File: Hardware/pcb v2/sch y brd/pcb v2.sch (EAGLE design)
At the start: 58 parts, among them J1 AVR_SPI_PRG_6PTH, J2 1981584-1, J3 HDMI, J4 JST-3, J5 HDMI, Q1 PMBT3904, Q2 PMBT3904, Q3 MC-306, U1 ATMEGA328P, U2 TXS0108EPWR-TSSOP20, U3 ADP3338AKCZ-3.3RL7, U4 DS1307SO8, Y1 CSTCE16M0V53-R0 16MHZ

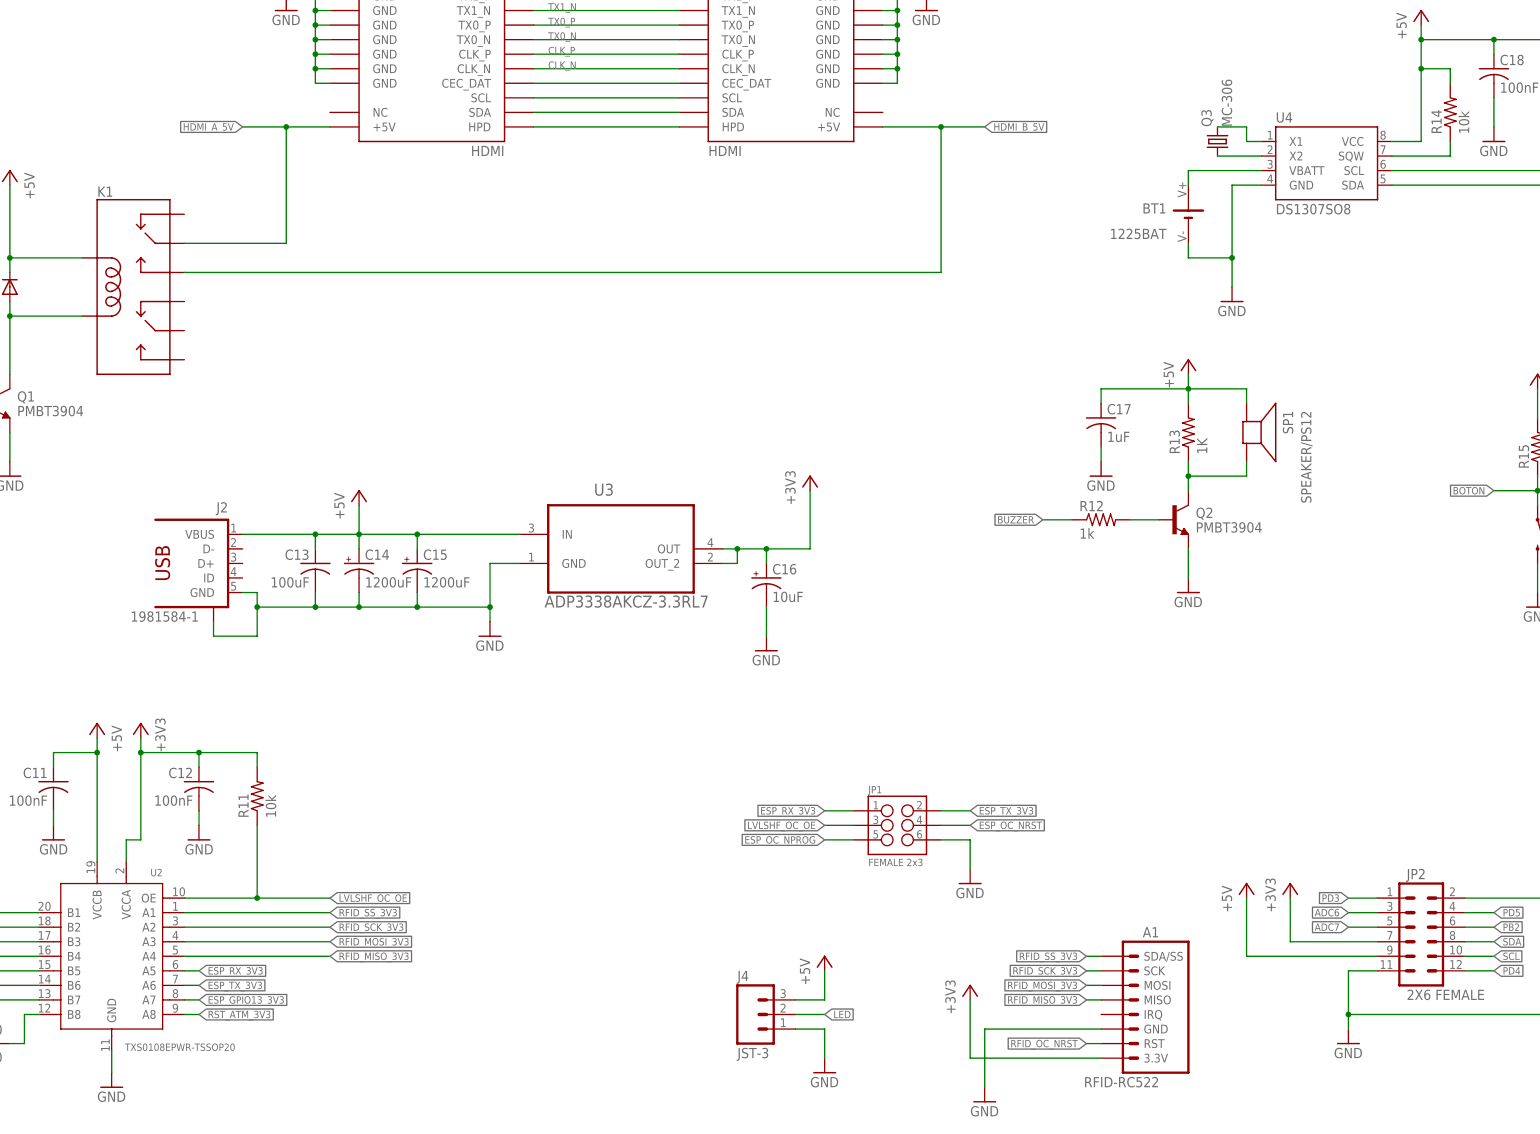
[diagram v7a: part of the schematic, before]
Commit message: Serigrafia arreglada
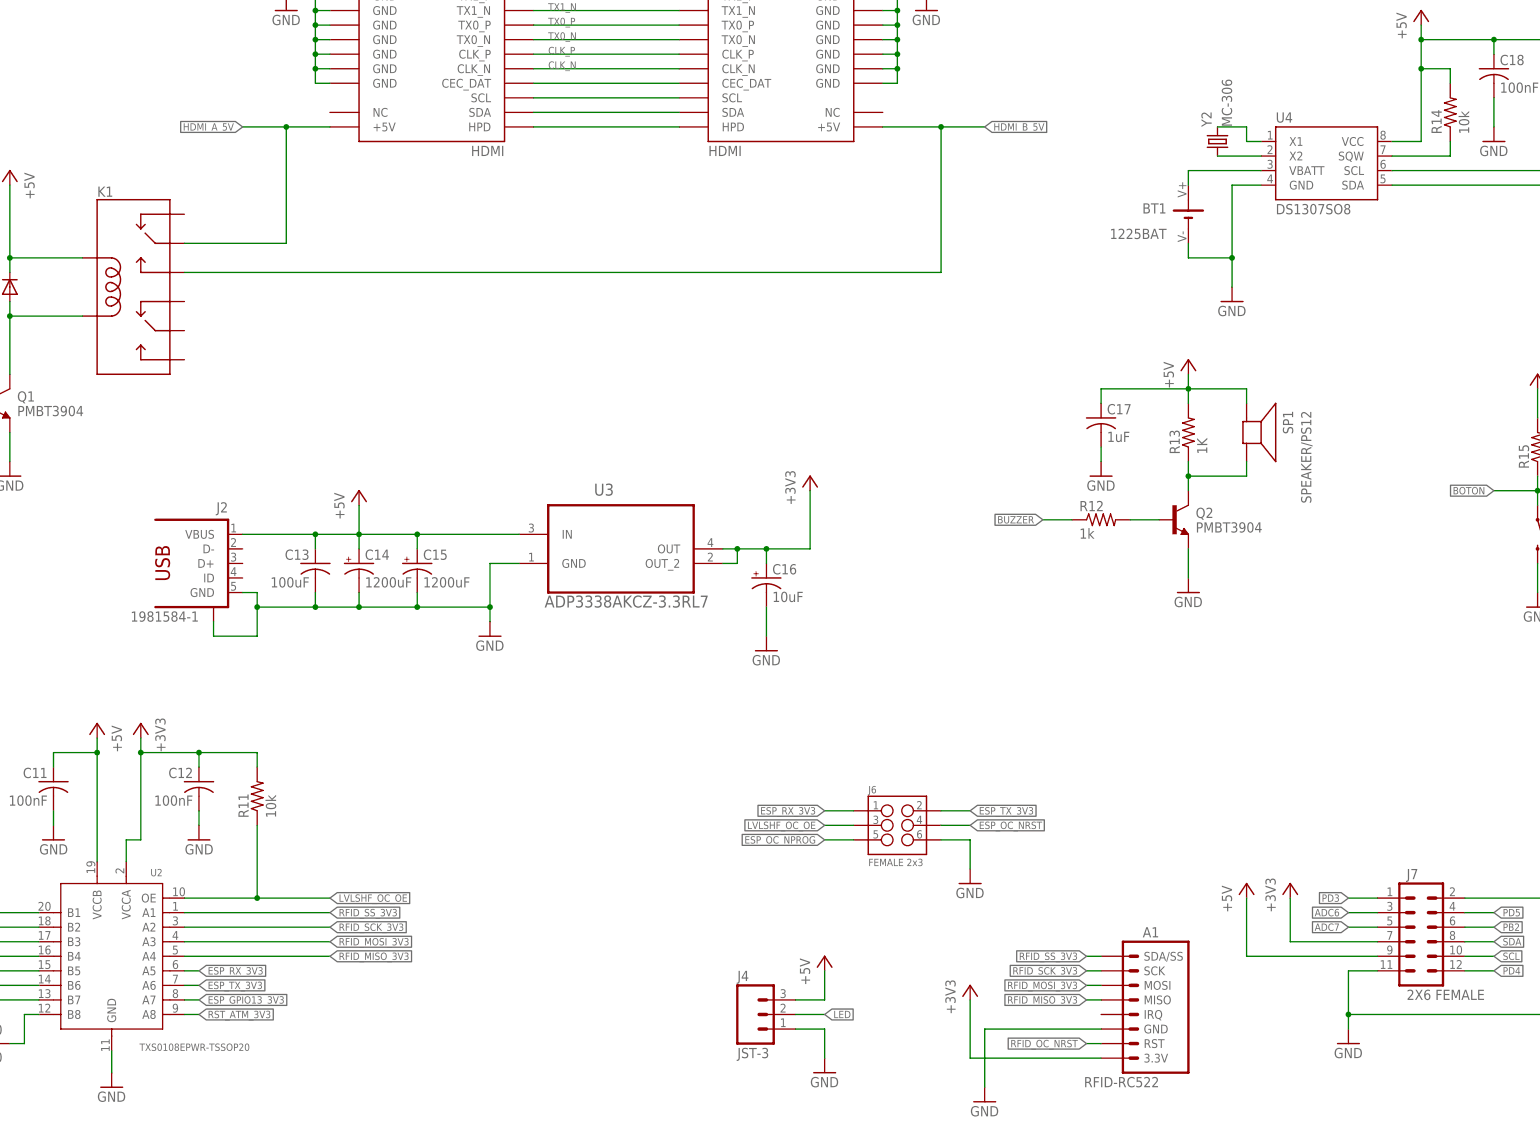
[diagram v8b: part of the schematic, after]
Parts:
- renumbered JP1 to J6, JP2 to J7, Q3 to Y2
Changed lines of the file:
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@@
 <part name="R1" library="rcl" deviceset="R-US_" device="R0805" value="NO(10k)"/>
 <part name="R10" library="rcl" deviceset="R-US_" device="R0805" value="0"/>
-<part name="JP1" library="SparkFun-Connectors" deviceset="M03X2" device="FEMALE" value="FEMALE 2x3"/>
-<part name="JP2" library="SparkFun-Connectors" deviceset="M06X2" device="PTH_FEMALE" value="2X6 FEMALE"/>
+<part name="J6" library="SparkFun-Connectors" deviceset="M03X2" device="FEMALE" value="FEMALE 2x3"/>
+<part name="J7" library="SparkFun-Connectors" deviceset="M06X2" device="PTH_FEMALE" value="2X6 FEMALE"/>
 <part name="GND22" library="supply1" deviceset="GND" device=""/>
 <part name="P+8" library="supply1" deviceset="+5V" device=""/>
@@
 <part name="GND17" library="supply1" deviceset="GND" device=""/>
 <part name="Y1" library="SmartPrj" deviceset="RESONATOR" device="MU" value="CSTCE16M0V53-R0 16MHZ"/>
-<part name="Q3" library="crystal" deviceset="MC-306" device=""/>
+<part name="Y2" library="crystal" deviceset="MC-306" device=""/>
 <part name="C14" library="rcl" deviceset="CPOL-US" device="UD-10X10" value="1200uF"/>
 <part name="C13" library="rcl" deviceset="C-US" device="C1206" value="100uF"/>
@@
 <instance part="U2" gate="G$1" x="193.04" y="20.32" smashed="yes" rot="MR0">
 <attribute name="NAME" x="201.93" y="34.29" size="1.27" layer="95" ratio="10" rot="MR0"/>
-<attribute name="VALUE" x="214.63" y="3.81" size="1.27" layer="96" ratio="10" rot="MR0"/>
+<attribute name="VALUE" x="217.17" y="3.81" size="1.27" layer="96" ratio="10" rot="MR0"/>
 </instance>
 <instance part="P+4" gate="1" x="190.5" y="60.96" rot="MR0"/>
@@
 <instance part="R1" gate="G$1" x="50.8" y="91.44" rot="R180"/>
 <instance part="R10" gate="G$1" x="170.18" y="5.08" rot="R180"/>
-<instance part="JP1" gate="G$1" x="330.2" y="43.18"/>
-<instance part="JP2" gate="G$1" x="419.1" y="17.78"/>
+<instance part="J6" gate="G$1" x="330.2" y="43.18"/>
+<instance part="J7" gate="G$1" x="419.1" y="17.78"/>
 <instance part="GND22" gate="1" x="408.94" y="5.08"/>
 <instance part="P+8" gate="1" x="391.16" y="33.02"/>
@@
 <attribute name="VALUE" x="55.88" y="27.94" size="1.778" layer="96" rot="R90"/>
 </instance>
-<instance part="Q3" gate="P" x="386.08" y="162.56" rot="R90"/>
+<instance part="Y2" gate="P" x="386.08" y="162.56" rot="R90"/>
 <instance part="C14" gate="G$1" x="236.22" y="88.9"/>
 <instance part="C13" gate="G$1" x="228.6" y="88.9" rot="MR0"/>
@@
 </segment>
 <segment>
-<pinref part="JP2" gate="G$1" pin="11"/>
+<pinref part="J7" gate="G$1" pin="11"/>
 <wire x1="414.02" y1="17.78" x2="408.94" y2="17.78" width="0.1524" layer="91"/>
 <pinref part="GND22" gate="1" pin="GND"/>
@@
 <junction x="408.94" y="10.16"/>
 <wire x1="444.5" y1="10.16" x2="444.5" y2="30.48" width="0.1524" layer="91"/>
-<pinref part="JP2" gate="G$1" pin="2"/>
+<pinref part="J7" gate="G$1" pin="2"/>
 <wire x1="444.5" y1="30.48" x2="429.26" y2="30.48" width="0.1524" layer="91"/>
 </segment>
@@
 </segment>
 <segment>
-<pinref part="JP1" gate="G$1" pin="6"/>
+<pinref part="J6" gate="G$1" pin="6"/>
 <pinref part="GND17" gate="1" pin="GND"/>
 <wire x1="337.82" y1="40.64" x2="342.9" y2="40.64" width="0.1524" layer="91"/>
@@
 </segment>
 <segment>
-<pinref part="JP2" gate="G$1" pin="9"/>
+<pinref part="J7" gate="G$1" pin="9"/>
 <pinref part="P+8" gate="1" pin="+5V"/>
 <wire x1="414.02" y1="20.32" x2="391.16" y2="20.32" width="0.1524" layer="91"/>
@@
 </segment>
 <segment>
-<pinref part="JP2" gate="G$1" pin="8"/>
+<pinref part="J7" gate="G$1" pin="8"/>
 <wire x1="429.26" y1="22.86" x2="434.34" y2="22.86" width="0.1524" layer="91"/>
 <label x="434.34" y="22.86" size="1.27" layer="95" xref="yes"/>
@@
 </segment>
 <segment>
-<pinref part="JP2" gate="G$1" pin="10"/>
+<pinref part="J7" gate="G$1" pin="10"/>
 <wire x1="429.26" y1="20.32" x2="434.34" y2="20.32" width="0.1524" layer="91"/>
 <label x="434.34" y="20.32" size="1.27" layer="95" xref="yes"/>
@@
 <pinref part="U4" gate="G$1" pin="X1"/>
 <wire x1="391.16" y1="162.56" x2="393.7" y2="162.56" width="0.1524" layer="91"/>
-<pinref part="Q3" gate="P" pin="2"/>
+<pinref part="Y2" gate="P" pin="2"/>
 </segment>
 </net>
@@
 <pinref part="U4" gate="G$1" pin="X2"/>
 <wire x1="386.08" y1="160.02" x2="393.7" y2="160.02" width="0.1524" layer="91"/>
-<pinref part="Q3" gate="P" pin="1"/>
+<pinref part="Y2" gate="P" pin="1"/>
 </segment>
 </net>
@@
 <pinref part="+3V37" gate="G$1" pin="+3V3"/>
 <wire x1="398.78" y1="30.48" x2="398.78" y2="22.86" width="0.1524" layer="91"/>
-<pinref part="JP2" gate="G$1" pin="7"/>
+<pinref part="J7" gate="G$1" pin="7"/>
 <wire x1="398.78" y1="22.86" x2="414.02" y2="22.86" width="0.1524" layer="91"/>
 </segment>
@@
 </segment>
 <segment>
-<pinref part="JP1" gate="G$1" pin="4"/>
+<pinref part="J6" gate="G$1" pin="4"/>
 <wire x1="337.82" y1="43.18" x2="342.9" y2="43.18" width="0.1524" layer="91"/>
 <label x="342.9" y="43.18" size="1.27" layer="95" xref="yes"/>
@@
 </segment>
 <segment>
-<pinref part="JP1" gate="G$1" pin="5"/>
+<pinref part="J6" gate="G$1" pin="5"/>
 <wire x1="322.58" y1="40.64" x2="317.5" y2="40.64" width="0.1524" layer="91"/>
 <label x="317.5" y="40.64" size="1.27" layer="95" rot="R180" xref="yes"/>
@@
 </segment>
 <segment>
-<pinref part="JP1" gate="G$1" pin="1"/>
+<pinref part="J6" gate="G$1" pin="1"/>
 <wire x1="322.58" y1="45.72" x2="317.5" y2="45.72" width="0.1524" layer="91"/>
 <label x="317.5" y="45.72" size="1.27" layer="95" rot="R180" xref="yes"/>
@@
 </segment>
 <segment>
-<pinref part="JP1" gate="G$1" pin="2"/>
+<pinref part="J6" gate="G$1" pin="2"/>
 <wire x1="337.82" y1="45.72" x2="342.9" y2="45.72" width="0.1524" layer="91"/>
 <label x="342.9" y="45.72" size="1.27" layer="95" xref="yes"/>
@@
 </segment>
 <segment>
-<pinref part="JP1" gate="G$1" pin="3"/>
+<pinref part="J6" gate="G$1" pin="3"/>
 <wire x1="322.58" y1="43.18" x2="317.5" y2="43.18" width="0.1524" layer="91"/>
 <label x="317.5" y="43.18" size="1.27" layer="95" rot="R180" xref="yes"/>
@@
 </segment>
 <segment>
-<pinref part="JP2" gate="G$1" pin="3"/>
+<pinref part="J7" gate="G$1" pin="3"/>
 <wire x1="414.02" y1="27.94" x2="408.94" y2="27.94" width="0.1524" layer="91"/>
 <label x="408.94" y="27.94" size="1.27" layer="95" rot="R180" xref="yes"/>
@@
 </segment>
 <segment>
-<pinref part="JP2" gate="G$1" pin="5"/>
+<pinref part="J7" gate="G$1" pin="5"/>
 <wire x1="414.02" y1="25.4" x2="408.94" y2="25.4" width="0.1524" layer="91"/>
 <label x="408.94" y="25.4" size="1.27" layer="95" rot="R180" xref="yes"/>
@@
 </segment>
 <segment>
-<pinref part="JP2" gate="G$1" pin="1"/>
+<pinref part="J7" gate="G$1" pin="1"/>
 <wire x1="414.02" y1="30.48" x2="408.94" y2="30.48" width="0.1524" layer="91"/>
 <label x="408.94" y="30.48" size="1.27" layer="95" rot="R180" xref="yes"/>
@@
 </segment>
 <segment>
-<pinref part="JP2" gate="G$1" pin="12"/>
+<pinref part="J7" gate="G$1" pin="12"/>
 <wire x1="429.26" y1="17.78" x2="434.34" y2="17.78" width="0.1524" layer="91"/>
 <label x="434.34" y="17.78" size="1.27" layer="95" xref="yes"/>
@@
 </segment>
 <segment>
-<pinref part="JP2" gate="G$1" pin="4"/>
+<pinref part="J7" gate="G$1" pin="4"/>
 <wire x1="429.26" y1="27.94" x2="434.34" y2="27.94" width="0.1524" layer="91"/>
 <label x="434.34" y="27.94" size="1.27" layer="95" xref="yes"/>
@@
 </segment>
 <segment>
-<pinref part="JP2" gate="G$1" pin="6"/>
+<pinref part="J7" gate="G$1" pin="6"/>
 <wire x1="429.26" y1="25.4" x2="434.34" y2="25.4" width="0.1524" layer="91"/>
 <label x="434.34" y="25.4" size="1.27" layer="95" xref="yes"/>
